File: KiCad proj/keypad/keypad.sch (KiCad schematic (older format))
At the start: 25 parts, among them J1 Keyboard_connector, Q1 Q_PNP_BEC, SW1 SW_Push_LED, SW2 SW_Push_LED, SW3 SW_Push_LED, SW4 SW_Push_LED, SW5 SW_Push_LED, SW6 SW_Push_LED, SW7 SW_Push_LED, SW8 SW_Push_LED

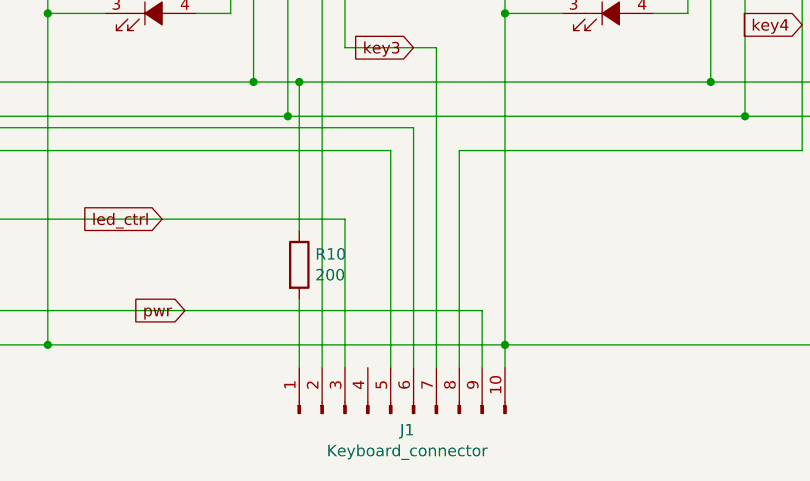
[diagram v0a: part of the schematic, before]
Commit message: Add labels to keyboard pins
Add labels to keyboard pins in order to have explicit key->port B pins
mapping
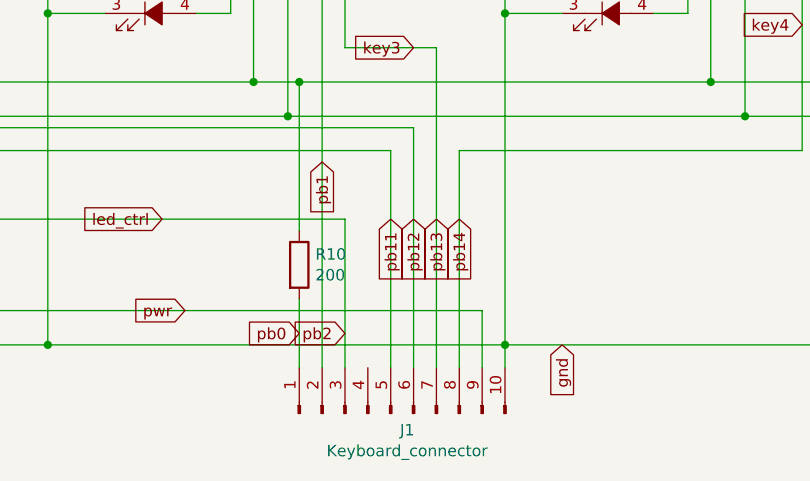
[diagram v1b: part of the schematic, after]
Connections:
- net pb0: now reaches J1.1 (Pin_1), R10.2
- net pb1: now reaches J1.2 (Pin_2), R11.2
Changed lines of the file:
@@
 Wire Wire Line
 	5150 3550 6950 3550
+Text GLabel 5150 4650 0    50   Input ~ 0
+pb0
+Text GLabel 5250 3900 3    50   Input ~ 0
+pb1
+Text GLabel 5350 4650 0    50   Input ~ 0
+pb2
+Text GLabel 6300 4700 3    50   Input ~ 0
+gnd
+Text GLabel 5550 4150 3    50   Input ~ 0
+pb11
+Text GLabel 5650 4150 3    50   Input ~ 0
+pb12
+Text GLabel 5750 4150 3    50   Input ~ 0
+pb13
+Text GLabel 5850 4150 3    50   Input ~ 0
+pb14
 $EndSCHEMATC
